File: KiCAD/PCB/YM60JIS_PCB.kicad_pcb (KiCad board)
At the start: 2 copper layers, 285.1 x 94.6 mm, 173 parts, among them J1 TYPE-C-31-M-12, SW1 SW_Push, SW10 SW_Push, SW11 SW_Push, SW12 SW_Push, SW13 SW_Push, SW14 SW_Push, SW15 SW_Push, SW16 SW_Push, SW17 SW_Push, SW18 SW_Push, SW19 SW_Push, SW2 SW_Push, SW20 SW_Push, SW21 SW_Push, SW22 SW_Push, SW23 SW_Push, SW24 SW_Push, SW25 SW_Push, SW26 SW_Push, SW27 SW_Push, SW28 SW_Push, SW29 Space, SW3 SW_Push, SW30 SW_Push, SW31 SW_Push, SW32 SW_Push, SW33 SW_Push, SW34 SW_Push, SW35 SW_Push, SW36 SW_Push, SW37 SW_Push, SW38 SW_Push, SW39 SW_Push, SW4 SW_Push, SW40 SW_Push, SW41 SW_Push, SW42 SW_Push, SW43 SW_Push, SW44 SW_Push, SW45 SW_Push, SW46 SW_Push, SW47 SW_Push, SW48 SW_Push, SW49 SW_Push, SW5 SW_Push, SW50 SW_Push, SW51 SW_Push, SW52 SW_Push, SW53 SW_Push, SW54 SW_Push, SW55 SW_Push, SW56 SW_Push, SW57 SW_Push, SW58 SW_Push, SW59 SW_Push, SW6 SW_Push, SW60 SW_Push, SW61 SW_Push, SW62 SW_Push, SW63 Yen, SW64 Backspace, SW65 ISOEnter, SW66 SW_Push, SW67 SW_Push, SW7 SW_Push, SW8 SW_Push, SW9 SW_Push, U1 XC6206P332MR, U2 SMF05CT1G, U3 RP2040, U4 W25Q16JVUXIQ, Y1 X322512MSB4SI

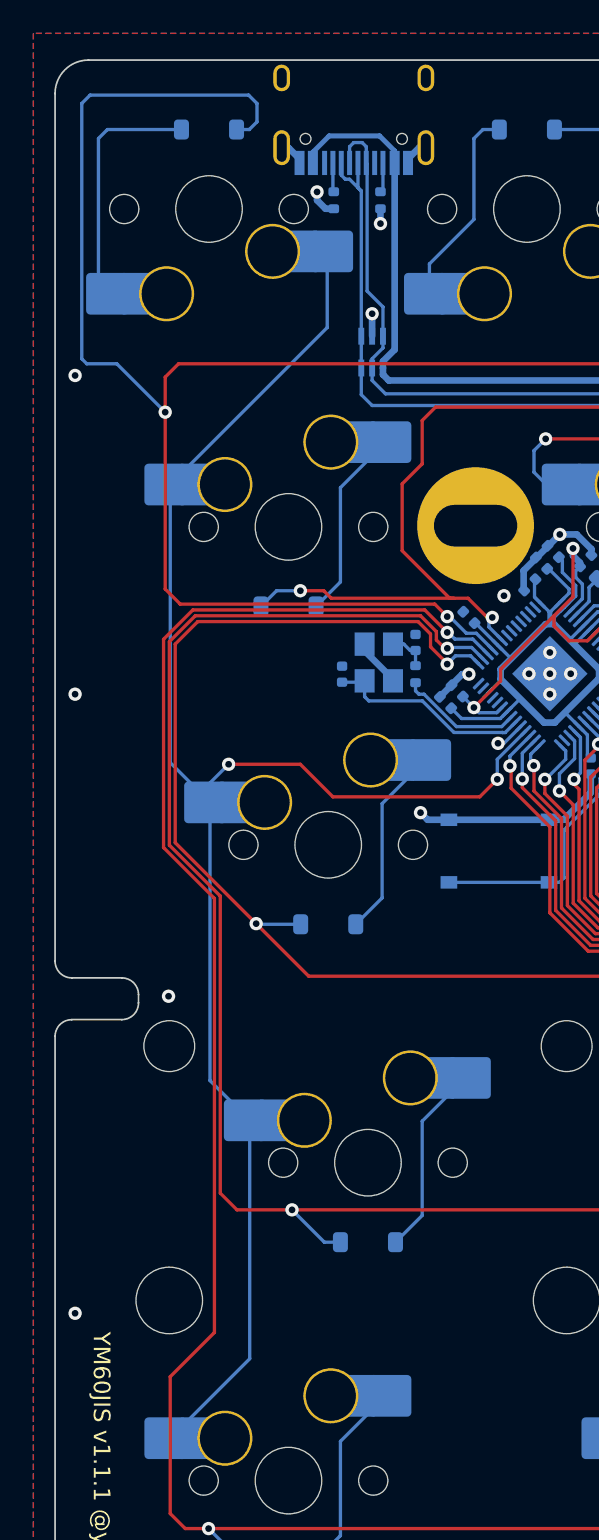
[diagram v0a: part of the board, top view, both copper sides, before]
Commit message: COL列配線を微調整
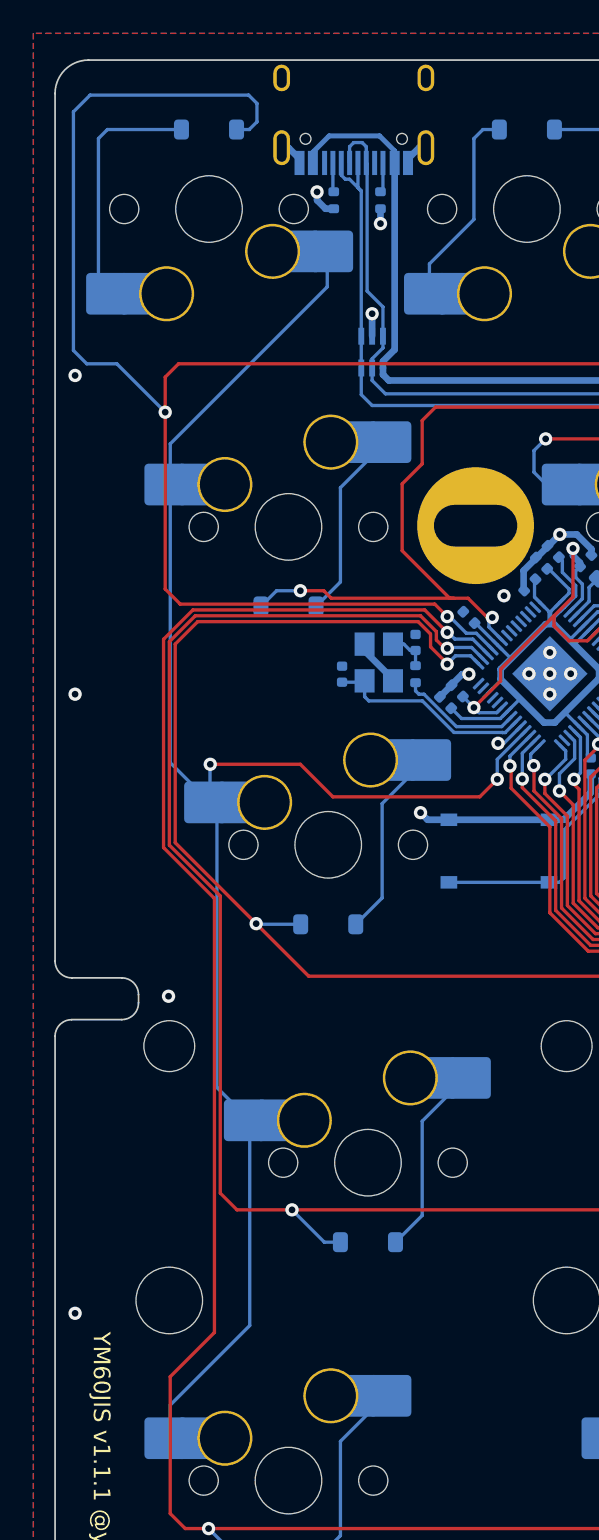
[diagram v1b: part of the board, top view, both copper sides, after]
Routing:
- net COL0: track 102.7 -> 103.3 mm
